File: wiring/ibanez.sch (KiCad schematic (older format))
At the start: 14 parts, among them J1 AudioJack2, SW1 SW_DPDT_x2, SW2 SW_DPDT_x2, SW3 SW_DPDT_x2, SW4 SW_DPDT_x2, SW5 SW_DPDT_x2, SW6 SW_DPDT_x2

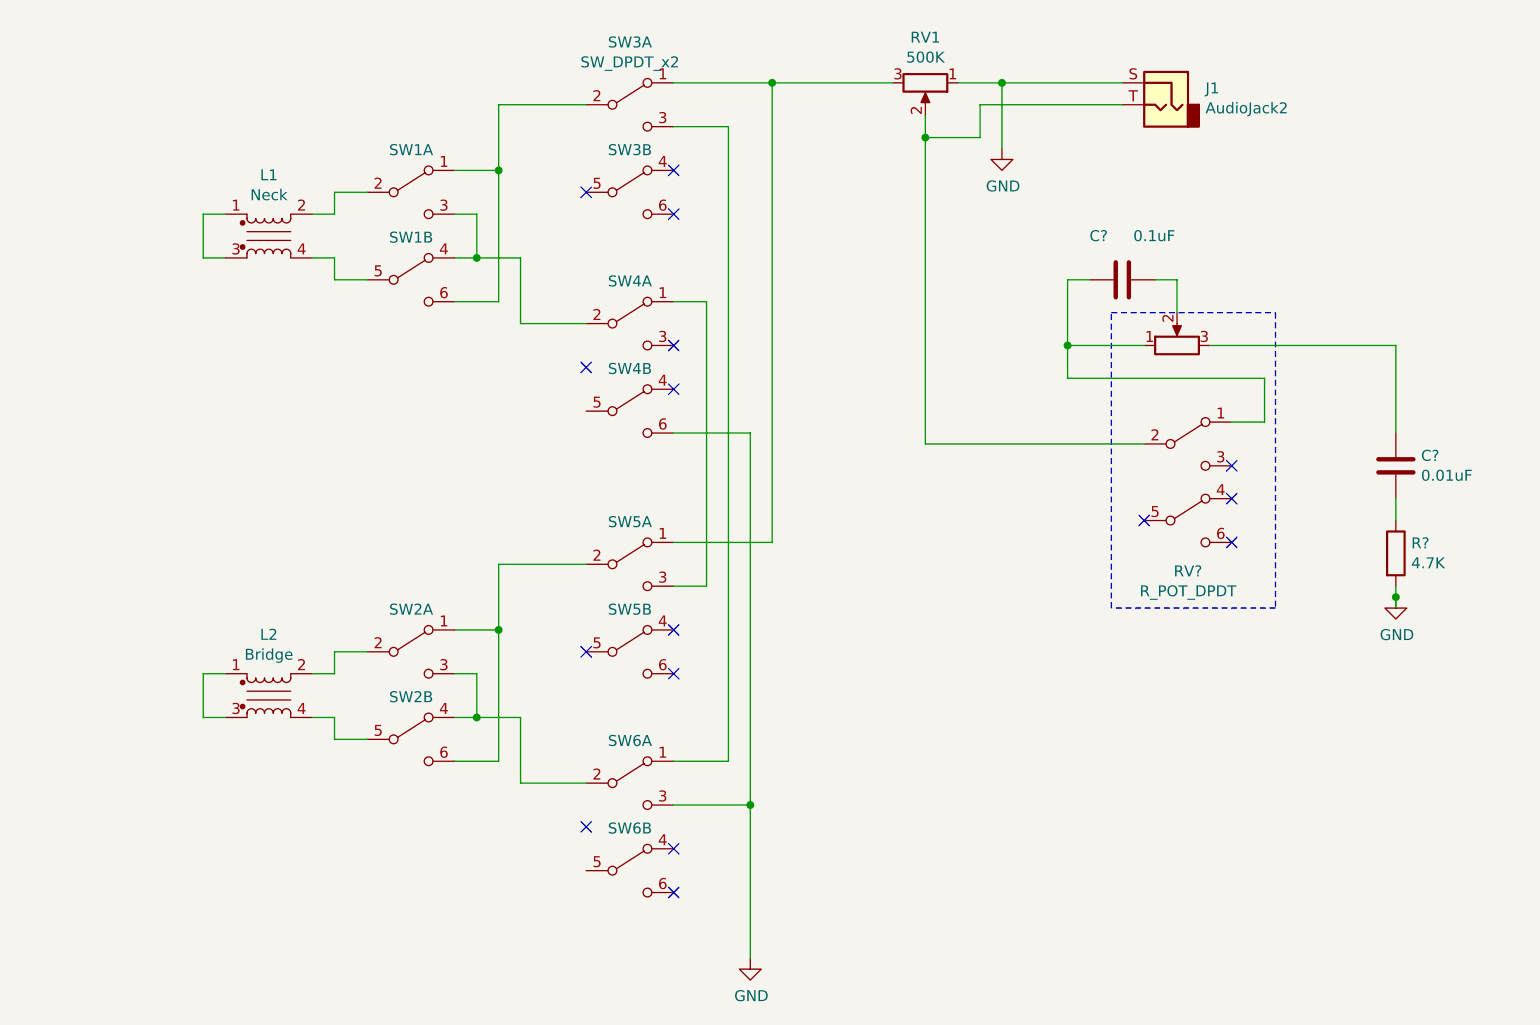
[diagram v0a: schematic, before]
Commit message: Update schematic following coil split switch mod
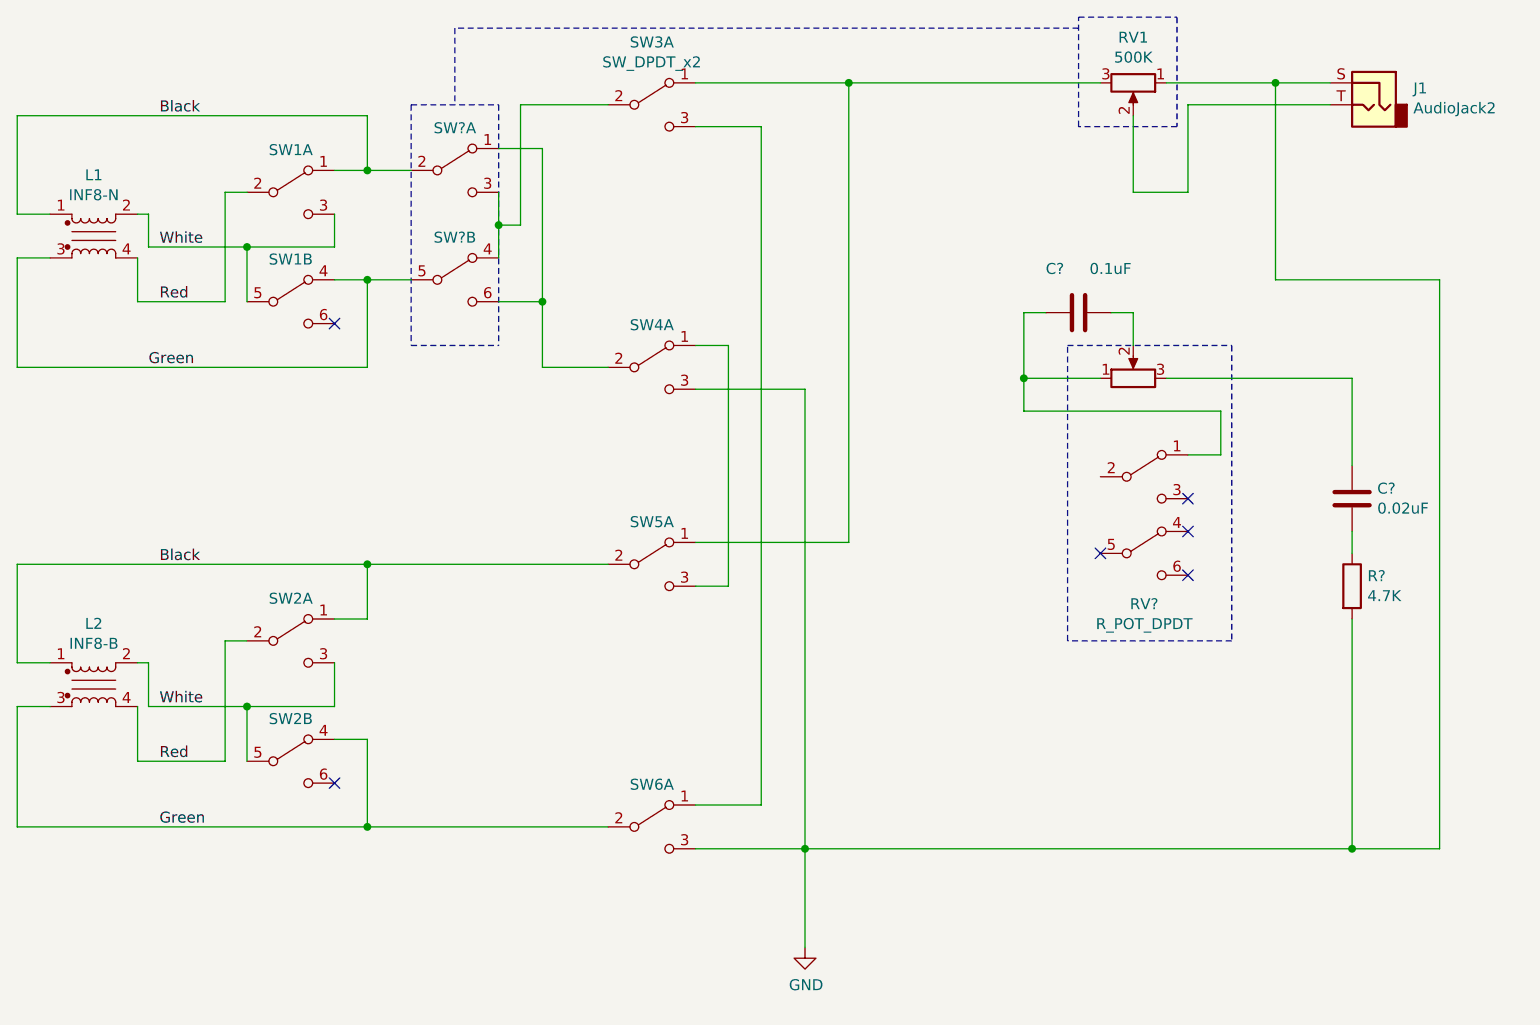
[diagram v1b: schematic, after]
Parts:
- removed unit 2 of SW3
- removed unit 2 of SW4
- removed unit 2 of SW5
- removed unit 2 of SW6
- added SW? (x2): SW_DPDT_x2, symbol Switch:SW_DPDT_x2
- C?: value 0.01uF -> 0.02uF
- L1: value Neck -> INF8-N
- L2: value Bridge -> INF8-B
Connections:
- net GND: now also SW4.3 (C)
- net Black: now reaches L1.1
- net Black: now also L2.1, SW1.1 (A), SW2.1 (A), SW5.2 (B), SW?.2 (B); no longer L1.3
- net Red: now reaches SW1.2 (B)
- net Red: now also L1.4, L2.4, SW2.2 (B); no longer L1.2
- net White: now reaches SW1.5 (B)
- net White: now also L1.2, L2.2, SW1.3 (C), SW2.3 (C), SW2.5 (B); no longer L1.4
- net Green: now reaches L2.3
- net Green: now also L1.3, SW1.4 (A), SW2.4 (A), SW6.2 (B), SW?.5 (B); no longer L2.1
- net at J1.T, RV1.2: no longer RV?.2 (B)
- new net: SW3.2 (B), SW?.3 (C), SW?.4 (A)
- new net: SW4.2 (B), SW?.1 (A), SW?.6 (C)
- now unconnected: SW1.6 (C), SW2.6 (C)
- no-connect marks 16 -> 6
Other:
- moved on the sheet: C?, J1, L1, L2, R?, RV1, RV?, SW1A, SW1B, SW2A, SW2B, SW3A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

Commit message: update schematic.  add pictures
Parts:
- gave numbers to parts that had none: 2
- renumbered SW3 to SW2, SW4 to SW3, SW5 to SW4, SW6 to SW5, SW1 to SW6, SW2 to SW7
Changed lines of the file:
@@
 $EndComp
 $Comp
-L Switch:SW_DPDT_x2 SW2
+L Switch:SW_DPDT_x2 SW7
 U 1 1 5C480077
 P 2650 4550
-F 0 "SW2" H 2650 4743 50  0000 C CNN
+F 0 "SW7" H 2650 4743 50  0000 C CNN
 F 1 "SW_DPDT_x2" H 2650 4744 50  0001 C CNN
 F 2 "" H 2650 4550 50  0001 C CNN
@@
 $EndComp
 $Comp
-L Switch:SW_DPDT_x2 SW2
+L Switch:SW_DPDT_x2 SW7
 U 2 1 5C48011F
 P 2650 5100
-F 0 "SW2" H 2650 5293 50  0000 C CNN
+F 0 "SW7" H 2650 5293 50  0000 C CNN
 F 1 "SW_DPDT_x2" H 2650 5294 50  0001 C CNN
 F 2 "" H 2650 5100 50  0001 C CNN
@@
 $EndComp
 $Comp
-L Switch:SW_DPDT_x2 SW1
+L Switch:SW_DPDT_x2 SW6
 U 1 1 5C480550
 P 2650 2500
-F 0 "SW1" H 2650 2693 50  0000 C CNN
+F 0 "SW6" H 2650 2693 50  0000 C CNN
 F 1 "SW_DPDT_x2" H 2650 2694 50  0001 C CNN
 F 2 "" H 2650 2500 50  0001 C CNN
@@
 $EndComp
 $Comp
-L Switch:SW_DPDT_x2 SW1
+L Switch:SW_DPDT_x2 SW6
 U 2 1 5C480556
 P 2650 3000
-F 0 "SW1" H 2650 3193 50  0000 C CNN
+F 0 "SW6" H 2650 3193 50  0000 C CNN
 F 1 "SW_DPDT_x2" H 2650 3194 50  0001 C CNN
 F 2 "" H 2650 3000 50  0001 C CNN
@@
 $EndComp
 $Comp
-L Switch:SW_DPDT_x2 SW3
+L Switch:SW_DPDT_x2 SW2
 U 1 1 5C480932
 P 4300 2100
-F 0 "SW3" H 4300 2385 50  0000 C CNN
-F 1 "SW_DPDT_x2" H 4300 2294 50  0000 C CNN
+F 0 "SW2" H 4300 2385 50  0000 C CNN
+F 1 "SW_DPDT_x2" H 4300 2294 50  0001 C CNN
 F 2 "" H 4300 2100 50  0001 C CNN
 F 3 "" H 4300 2100 50  0001 C CNN
@@
 $EndComp
 $Comp
-L Switch:SW_DPDT_x2 SW4
+L Switch:SW_DPDT_x2 SW3
 U 1 1 5C480A74
 P 4300 3300
-F 0 "SW4" H 4300 3493 50  0000 C CNN
+F 0 "SW3" H 4300 3493 50  0000 C CNN
 F 1 "SW_DPDT_x2" H 4300 3494 50  0001 C CNN
 F 2 "" H 4300 3300 50  0001 C CNN
@@
 $EndComp
 $Comp
-L Switch:SW_DPDT_x2 SW5
+L Switch:SW_DPDT_x2 SW4
 U 1 1 5C480EA8
 P 4300 4200
-F 0 "SW5" H 4300 4393 50  0000 C CNN
+F 0 "SW4" H 4300 4393 50  0000 C CNN
 F 1 "SW_DPDT_x2" H 4300 4394 50  0001 C CNN
 F 2 "" H 4300 4200 50  0001 C CNN
@@
 $EndComp
 $Comp
-L Switch:SW_DPDT_x2 SW6
+L Switch:SW_DPDT_x2 SW5
 U 1 1 5C480EB6
 P 4300 5400
-F 0 "SW6" H 4300 5593 50  0000 C CNN
+F 0 "SW5" H 4300 5593 50  0000 C CNN
 F 1 "SW_DPDT_x2" H 4300 5594 50  0001 C CNN
 F 2 "" H 4300 5400 50  0001 C CNN
@@
 	5000 5500 5000 5950
 $Comp
-L ibanez:R_POT_DPDT RV?
+L ibanez:R_POT_DPDT RV8
 U 1 1 5C6DAB04
 P 6550 3600
-F 0 "RV?" H 6550 2818 50  0000 C CNN
-F 1 "R_POT_DPDT" H 6550 2727 50  0000 C CNN
+F 0 "RV8" H 6550 2818 50  0000 C CNN
+F 1 "R_POT_DPDT" H 6550 2727 50  0001 C CNN
 F 2 "" V 6500 3850 50  0001 C CNN
 F 3 "~" V 6500 3850 50  0001 C CNN
@@
 Black
 $Comp
-L Switch:SW_DPDT_x2 SW?
+L Switch:SW_DPDT_x2 SW1
 U 1 1 5C70666A
 P 3400 2400
-F 0 "SW?" H 3400 2593 50  0000 C CNN
+F 0 "SW1" H 3400 2593 50  0000 C CNN
 F 1 "SW_DPDT_x2" H 3400 2594 50  0001 C CNN
 F 2 "" H 3400 2400 50  0001 C CNN
@@
 $EndComp
 $Comp
-L Switch:SW_DPDT_x2 SW?
+L Switch:SW_DPDT_x2 SW1
 U 2 1 5C706671
 P 3400 2900
-F 0 "SW?" H 3400 3093 50  0000 C CNN
+F 0 "SW1" H 3400 3093 50  0000 C CNN
 F 1 "SW_DPDT_x2" H 3400 3094 50  0001 C CNN
 F 2 "" H 3400 2900 50  0001 C CNN
@@
 Wire Wire Line
 	2350 4550 2450 4550
+Wire Notes Line
+	2400 2250 2900 2250
+Wire Notes Line
+	2900 2250 2900 3200
+Wire Notes Line
+	2900 3200 2400 3200
+Wire Notes Line
+	2400 3200 2400 2250
+Wire Notes Line
+	2400 4300 2900 4300
+Wire Notes Line
+	2900 4300 2900 5300
+Wire Notes Line
+	2900 5300 2400 5300
+Wire Notes Line
+	2400 5300 2400 4300
 $EndSCHEMATC

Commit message: local mods, was updating wiring
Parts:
- RV8: symbol ibanez:R_POT_DPDT -> ibanez-rescue:R_POT_DPDT-ibanez
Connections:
- net at RV1.3, SW2.1 (A), SW4.1 (A): now also RV8.2 (B)
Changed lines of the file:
@@
 	5000 5500 5000 5950
 $Comp
-L ibanez:R_POT_DPDT RV8
+L ibanez-rescue:R_POT_DPDT-ibanez RV8
 U 1 1 5C6DAB04
 P 6550 3600
@@
 Connection ~ 3000 5400
 Wire Wire Line
-	5200 2000 5200 4100
+	5200 2000 5200 3800
 Wire Wire Line
 	6500 2150 6500 2500
@@
 Wire Notes Line
 	2400 5300 2400 4300
+Wire Wire Line
+	6350 3800 5200 3800
+Connection ~ 5200 3800
+Wire Wire Line
+	5200 3800 5200 4100
 $EndSCHEMATC
